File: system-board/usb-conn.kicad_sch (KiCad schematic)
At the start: 4 parts, among them J10 217183-0001

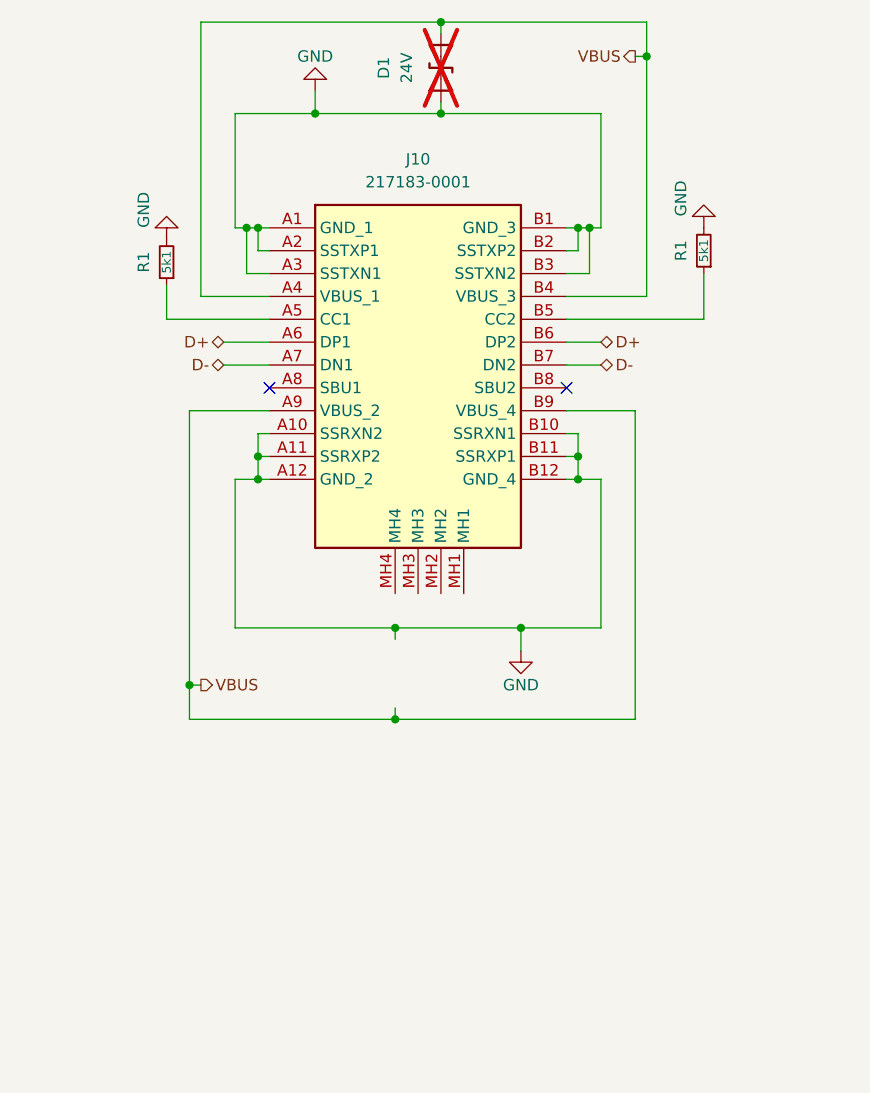
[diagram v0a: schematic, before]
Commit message: Redo system-board PCB to use fewer connectors
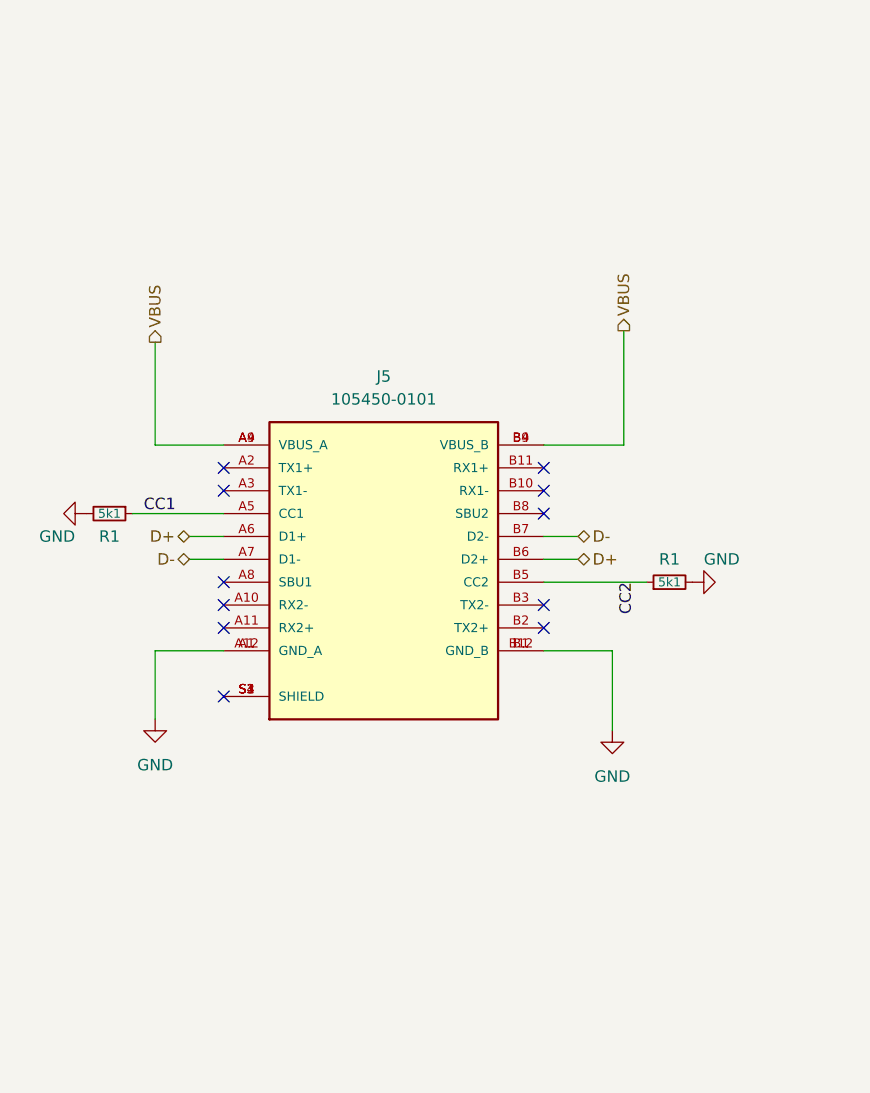
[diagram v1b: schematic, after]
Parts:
- removed D1: 24V, Diode_SMD:D_SMA, symbol Device:D_TVS
- removed J10: 217183-0001, Imports:Molex USB-C Horizontal 2171830001, symbol imports:217183-0001
- added J5: 105450-0101, Imports:AMPHENOL_12401832E402A, symbol imports:12401832E402A
- R1: digikey part number (none) -> 10-ERJ-U02F5101XTR-ND
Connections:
- net D+: now also J5.A6 (D1+), J5.B6 (D2+)
- net D-: now also J5.A7 (D1-), J5.B7 (D2-)
- net GND: now also J5.A1 (GND_A), J5.A12 (GND_A), J5.B1 (GND_B), J5.B12 (GND_B)
- net VBUS: now also J5.A4 (VBUS_A), J5.A9 (VBUS_A), J5.B4 (VBUS_B), J5.B9 (VBUS_B)
- net CC1: now reaches R1.1
- net CC1: now also J5.A5 (CC1)
- net CC2: now reaches R1.1
- net CC2: now also J5.B5 (CC2)
- new net: J5.S1 (SHIELD), J5.S2 (SHIELD), J5.S3 (SHIELD), J5.S4 (SHIELD)
- no-connect marks 2 -> 11
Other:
- moved on the sheet: R1

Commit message: Yet another PCB Revision
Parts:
- added IC5: HSP061-2M6, Imports:SON50P100X145X65-6N-D, symbol imports:HSP061-2M6
- J5: DESCRIPTION USB Shielded I/O Receptacle; Type C; Right Angle; Surface M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 -> (none); MANUFACTURER Amphenol -> (none); MAXIMUM_PACKAGE_HIEGHT 3.28mm -> (none); PARTREV X2 -> (none); package (none) -> SMD
- R1: MPN (none) -> ERJ-U02F5101X; package (none) -> 0402
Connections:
- net D+: now also IC5.3 (I/O2_1); no longer J5.A6 (D1+), J5.B6 (D2+)
- net D-: now also IC5.1 (I/O1_1); no longer J5.A7 (D1-), J5.B7 (D2-)
- net GND: now also IC5.2 (GND)
- net VBUS: now also IC5.5 (VBUS)
- new net RAW_D+: IC5.4 (I/O2_2), J5.A6 (D1+), J5.B6 (D2+)
- new net RAW_D-: IC5.6 (I/O1_2), J5.A7 (D1-), J5.B7 (D2-)
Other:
- moved on the sheet: R1

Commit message: Redo design again
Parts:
- renumbered IC5 to IC3, J5 to J7
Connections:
- net D+: now also IC3.1 (I/O1_1); no longer IC3.3 (I/O2_1)
- net D-: now also IC3.3 (I/O2_1); no longer IC3.1 (I/O1_1)
- net RAW_D+: now also IC3.6 (I/O1_2); no longer IC3.4 (I/O2_2)
- net RAW_D-: now also IC3.4 (I/O2_2); no longer IC3.6 (I/O1_2)
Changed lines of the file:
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@@
+    (stroke (width 0) (type default))
+  )
+  (wire (pts (xy 95.25 147.32) (xy 95.25 165.1))
     (stroke (width 0) (type default))
   )
@@
     (stroke (width 0) (type default))
   )
-  (wire (pts (xy 109.22 170.18) (xy 95.25 170.18))
-    (stroke (width 0) (type default))
-  )
   (wire (pts (xy 100.33 125.73) (xy 107.95 125.73))
     (stroke (width 0) (type default))
@@
     (stroke (width 0) (type default))
   )
+  (wire (pts (xy 104.14 170.18) (xy 109.22 170.18))
+    (stroke (width 0) (type default))
+  )
   (wire (pts (xy 143.51 125.73) (xy 151.13 125.73))
     (stroke (width 0) (type default))
@@
     (stroke (width 0) (type default))
   )
-  (wire (pts (xy 95.25 147.32) (xy 95.25 170.18))
-    (stroke (width 0) (type default))
-  )
   (wire (pts (xy 152.4 90.17) (xy 152.4 102.87))
     (stroke (width 0) (type default))
@@
     (stroke (width 0) (type default))
   )
-  (wire (pts (xy 109.22 165.1) (xy 104.14 165.1))
-    (stroke (width 0) (type default))
-  )
   (wire (pts (xy 104.14 148.59) (xy 177.8 148.59))
     (stroke (width 0) (type default))
@@
     (stroke (width 0) (type default))
   )
-  (wire (pts (xy 104.14 148.59) (xy 104.14 165.1))
+  (wire (pts (xy 109.22 165.1) (xy 95.25 165.1))
+    (stroke (width 0) (type default))
+  )
+  (wire (pts (xy 104.14 148.59) (xy 104.14 170.18))
     (stroke (width 0) (type default))
   )
@@
     (effects (font (size 1.27 1.27)) (justify right bottom))
   )
+  (hierarchical_label "D-" (shape bidirectional) (at 146.05 170.18 0) (fields_autoplaced)
+    (effects (font (size 1.27 1.27)) (justify left))
+  )
   (hierarchical_label "VBUS" (shape output) (at 152.4 90.17 90) (fields_autoplaced)
     (effects (font (size 1.27 1.27)) (justify left))
   )
-  (hierarchical_label "D-" (shape bidirectional) (at 146.05 165.1 0) (fields_autoplaced)
+  (hierarchical_label "D+" (shape bidirectional) (at 146.05 165.1 0) (fields_autoplaced)
     (effects (font (size 1.27 1.27)) (justify left))
   )
@@
     (effects (font (size 1.27 1.27)) (justify left))
   )
-  (hierarchical_label "D+" (shape bidirectional) (at 146.05 170.18 0) (fields_autoplaced)
-    (effects (font (size 1.27 1.27)) (justify left))
-  )
   (symbol (lib_id "Device:R_Small") (at 95.25 110.49 270) (unit 1)
     (in_bom yes) (on_board yes) (dnp no)
@@
         )
         (path "/54f22c46-3801-43f0-a916-fc0a05246fe7/6dfa3454-3420-46f1-8956-247d92060c23"
-          (reference "R23") (unit 1)
+          (reference "R18") (unit 1)
         )
       )
@@
   (symbol (lib_id "imports:HSP061-2M6") (at 142.24 165.1 0) (mirror y) (unit 1)
     (in_bom yes) (on_board yes) (dnp no)
-    (property "Reference" "IC5" (at 125.73 157.48 0)
+    (property "Reference" "IC3" (at 125.73 157.48 0)
       (effects (font (size 1.27 1.27)))
     )
@@
       (project "system-board"
         (path "/54f22c46-3801-43f0-a916-fc0a05246fe7/6dfa3454-3420-46f1-8956-247d92060c23"
-          (reference "IC5") (unit 1)
+          (reference "IC3") (unit 1)
         )
       )
@@
   (symbol (lib_id "imports:12401832E402A") (at 125.73 115.57 0) (unit 1)
     (in_bom yes) (on_board yes) (dnp no) (fields_autoplaced)
-    (property "Reference" "J5" (at 125.73 95.25 0)
+    (property "Reference" "J7" (at 125.73 95.25 0)
       (effects (font (size 1.27 1.27)))
     )
@@
       (project "system-board"
         (path "/54f22c46-3801-43f0-a916-fc0a05246fe7/6dfa3454-3420-46f1-8956-247d92060c23"
-          (reference "J5") (unit 1)
+          (reference "J7") (unit 1)
         )
       )
@@
   (symbol (lib_id "power:GND") (at 100.33 133.35 0) (unit 1)
     (in_bom yes) (on_board yes) (dnp no) (fields_autoplaced)
-    (property "Reference" "#PWR047" (at 100.33 139.7 0)
+    (property "Reference" "#PWR052" (at 100.33 139.7 0)
       (effects (font (size 1.27 1.27)) hide)
     )
@@
       (project "system-board"
         (path "/54f22c46-3801-43f0-a916-fc0a05246fe7/6dfa3454-3420-46f1-8956-247d92060c23"
-          (reference "#PWR047") (unit 1)
+          (reference "#PWR052") (unit 1)
         )
       )
@@
         )
         (path "/54f22c46-3801-43f0-a916-fc0a05246fe7/6dfa3454-3420-46f1-8956-247d92060c23"
-          (reference "#PWR060") (unit 1)
+          (reference "#PWR050") (unit 1)
         )
       )
@@
   (symbol (lib_id "power:GND") (at 151.13 134.62 0) (unit 1)
     (in_bom yes) (on_board yes) (dnp no) (fields_autoplaced)
-    (property "Reference" "#PWR044" (at 151.13 140.97 0)
+    (property "Reference" "#PWR053" (at 151.13 140.97 0)
       (effects (font (size 1.27 1.27)) hide)
     )
@@
       (project "system-board"
         (path "/54f22c46-3801-43f0-a916-fc0a05246fe7/6dfa3454-3420-46f1-8956-247d92060c23"
-          (reference "#PWR044") (unit 1)
+          (reference "#PWR053") (unit 1)
         )
       )
@@
   (symbol (lib_id "power:GND") (at 153.67 167.64 90) (unit 1)
     (in_bom yes) (on_board yes) (dnp no)
-    (property "Reference" "#PWR063" (at 160.02 167.64 0)
+    (property "Reference" "#PWR054" (at 160.02 167.64 0)
       (effects (font (size 1.27 1.27)) hide)
     )
@@
       (project "system-board"
         (path "/54f22c46-3801-43f0-a916-fc0a05246fe7/6dfa3454-3420-46f1-8956-247d92060c23"
-          (reference "#PWR063") (unit 1)
+          (reference "#PWR054") (unit 1)
         )
       )
@@
         )
         (path "/54f22c46-3801-43f0-a916-fc0a05246fe7/6dfa3454-3420-46f1-8956-247d92060c23"
-          (reference "R24") (unit 1)
+          (reference "R19") (unit 1)
         )
       )
@@
         )
         (path "/54f22c46-3801-43f0-a916-fc0a05246fe7/6dfa3454-3420-46f1-8956-247d92060c23"
-          (reference "#PWR061") (unit 1)
-        )
-      )
+          (reference "#PWR051") (unit 1)
+        )
+      )
